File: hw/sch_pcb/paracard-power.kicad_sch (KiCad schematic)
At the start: 1 part, among them P3 BTH-030-01-F-D-A

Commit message: Update schematics. Preparation to resolve #2.
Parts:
- P3: footprint CONN_SAMTEC_BTH_60 -> Mlab_CON:SAMTEC-BTH-030-01-X-D-A; symbol adapteva_kicad:CONN_SAMTEC_BTH_60 -> MLAB_CONNECTORS:CONN_SAMTEC_BTH_030
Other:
- company: ORBISYS www.orbisys.sk -> MLAB.cz
- title: MPPB01A -> MPPB01B
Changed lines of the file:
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@@
   (paper "B")
   (title_block
-    (title "MPPB01A")
-    (date "09 May 2014")
-    (rev "REV 0.1")
-    (company "ORBISYS www.orbisys.sk")
+    (title "MPPB01B")
+    (date "2022-03-24")
+    (company "MLAB.cz")
     (comment 1 "VERSION 1")
     (comment 2 "Paralella reduction board")
-    (comment 3 "Maksim Rezenov, Jakub kakona")
+    (comment 3 "Maksim Rezenov, Jakub Kakona")
   )
   (junction (at 214.63 116.84) (diameter 0) (color 0 0 0 0)
@@
     (pin "1")
   )
-  (symbol (lib_id "adapteva_kicad:CONN_SAMTEC_BTH_60") (at 232.41 128.27 0) (unit 1)
+  (symbol (lib_id "MLAB_CONNECTORS:CONN_SAMTEC_BTH_030") (at 232.41 128.27 0) (unit 1)
     (in_bom yes) (on_board yes)
     (property "Reference" "P3" (id 0) (at 232.41 85.09 0)
@@
       (effects (font (size 1.524 1.524)))
     )
-    (property "Footprint" "CONN_SAMTEC_BTH_60" (id 2) (at 234.95 128.27 90)
+    (property "Footprint" "Mlab_CON:SAMTEC-BTH-030-01-X-D-A" (id 2) (at 234.95 128.27 90)
       (effects (font (size 1.524 1.524)) hide)
     )
-    (property "Datasheet" "" (id 3) (at 234.95 105.41 0)
+    (property "Datasheet" "https://cz.mouser.com/datasheet/2/527/bth-2498158.pdf" (id 3) (at 234.95 105.41 0)
       (effects (font (size 1.524 1.524)) hide)
     )

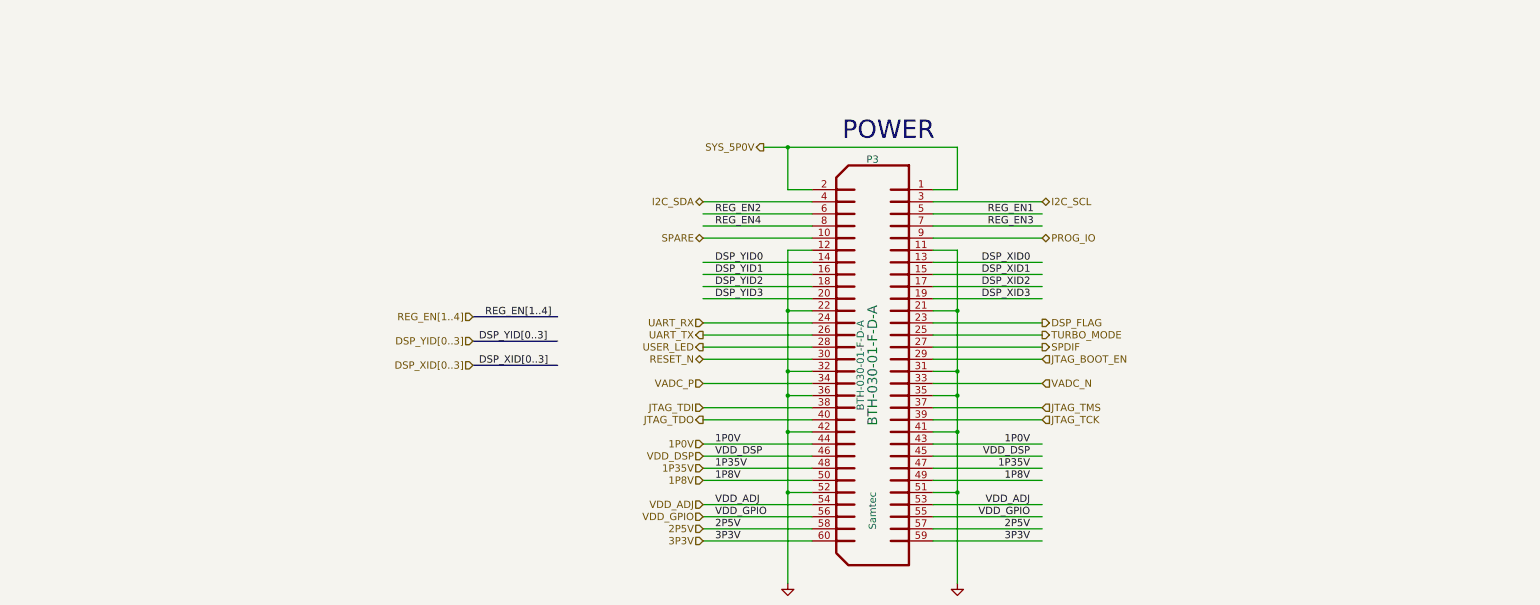
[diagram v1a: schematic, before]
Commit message: Adding pull-up resistor to resolve #1.
Geometric preparation for #2.
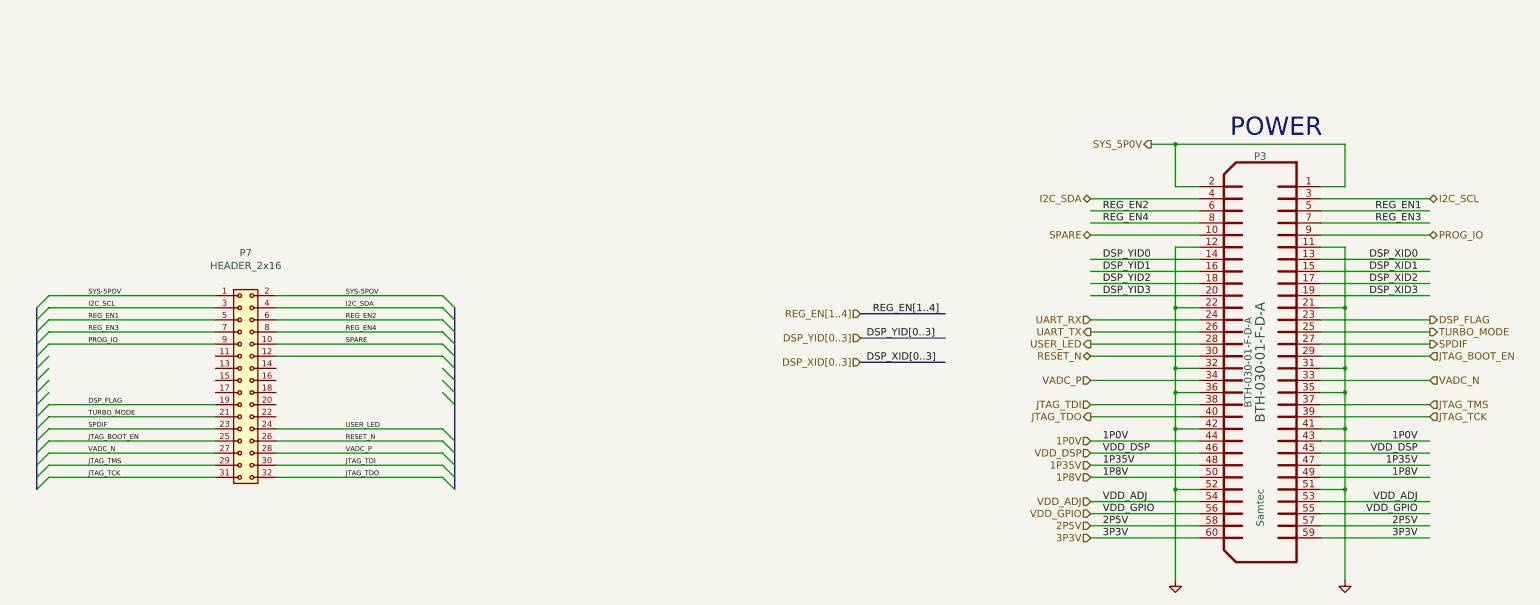
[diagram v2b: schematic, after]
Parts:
- added P7: HEADER_2x16, Mlab_Pin_Headers:Straight_2x16, symbol MLAB_HEADER:HEADER_2x16
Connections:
- net DSP_FLAG: now also P7.19
- net I2C_SCL: now also P7.3
- net I2C_SDA: now also P7.4
- net JTAG_BOOT_EN: now also P7.25
- net JTAG_TCK: now also P7.31
- net JTAG_TDI: now also P7.30
- net JTAG_TDO: now also P7.32
- net JTAG_TMS: now also P7.29
- net PROG_IO: now also P7.9
- net REG_EN1: now also P7.5
- net REG_EN2: now also P7.6
- net REG_EN3: now also P7.7
- net REG_EN4: now also P7.8
- net RESET_N: now also P7.26
- net SPARE: now also P7.10
- net SPDIF: now also P7.23
- net TURBO_MODE: now also P7.21
- net USER_LED: now also P7.24
- net VADC_N: now also P7.27
- net VADC_P: now also P7.28
- new net SYS-5POV: P7.1, P7.2
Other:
- moved on the sheet: P3

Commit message: Improve connector pinout #2
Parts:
- added P11: HEADER_2x05_PARALLEL, Mlab_Pin_Headers:Straight_2x05, symbol MLAB_HEADER:HEADER_2x05_PARALLEL
- added R3: 10k, Resistor_SMD:R_0805_2012Metric_Pad1.20x1.40mm_HandSolder, symbol paracard-template-rescue:R-device
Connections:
- net 2P5V: now also P7.12
- net 3P3V: now also P7.6
- net GND: now also P7.5, P11.1, P11.10, P11.2, P11.9
- net I2C_SCL: now also P11.3, P11.4; no longer P7.3
- net I2C_SDA: now also P11.7, P11.8; no longer P7.4
- net REG_EN1: no longer P7.5
- net REG_EN2: no longer P7.6
- net SPARE: no longer P3.10 (P10)
- net SYS-5POV: now also P11.5, P11.6
- net UART_RX: now also P7.3, R3.2
- net UART_TX: now also P7.4
- net VDD_ADJ: now also P7.14, R3.1
- net VDD_GPIO: now also P7.16
- no-connect marks 0 -> 1

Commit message: routing cest ke konektoru
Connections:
- net DSP_FLAG: now also P7.31; no longer P7.19
- net JTAG_TCK: now also P7.19; no longer P7.31
- net JTAG_TMS: now also P7.23; no longer P7.29
- net SPDIF: now also P7.27; no longer P7.23
- net TURBO_MODE: now also P7.29; no longer P7.21
- net VADC_N: now also P7.21; no longer P7.27
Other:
- moved on the sheet: P7, R3

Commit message: uprava pinoutu konektoru
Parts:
- removed P7: HEADER_2x16, Mlab_Pin_Headers:Straight_2x16, symbol MLAB_HEADER:HEADER_2x16
- added P7: HEADER_2x13, Mlab_Pin_Headers:Straight_2x13, symbol MLAB_HEADER:HEADER_2x13
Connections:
- net 2P5V: now also P7.12
- net 3P3V: now also P7.6, P7.8
- net DSP_FLAG: now also P7.25
- net GND: now also P7.5, P7.7
- net JTAG_BOOT_EN: now also P7.19
- net JTAG_TCK: now also P7.13
- net JTAG_TDI: now also P7.14
- net JTAG_TDO: now also P7.16
- net JTAG_TMS: now also P7.15
- net PROG_IO: now also P7.11
- net REG_EN3: now also P7.9
- net REG_EN4: now also P7.10
- net RESET_N: now also P7.20
- net SPDIF: now also P7.21
- net SYS-5POV: now also P7.1, P7.2
- net TURBO_MODE: now also P7.23
- net UART_RX: now also P7.3
- net UART_TX: now also P7.4
- net USER_LED: now also P7.18
- net VADC_N: now also P7.17
- net VADC_P: now also P7.22
- net VDD_ADJ: now also P7.24
- net VDD_GPIO: now also P7.26
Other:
- moved on the sheet: R3

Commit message: Routovani cesticek, uprava pinoutu
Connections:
- net SYS-5POV is gone; now on net SYS_5P0V: P11.5, P11.6, P7.1, P7.2
- net 3P3V: now also P7.3, P7.4; no longer P7.6, P7.8
- net GND: now also P7.6; no longer P7.7
- net SPDIF: now also P7.17; no longer P7.21
- net UART_RX: now also P7.7; no longer P7.3
- net UART_TX: now also P7.8; no longer P7.4
- net VADC_N: now also P7.21; no longer P7.17

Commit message: pridani UST_ID
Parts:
- R3: UST_ID (none) -> 5c70984612875079b91f899f
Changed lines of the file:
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@@
+      (effects (font (size 1.27 1.27)) hide)
+    )
+    (property "UST_ID" "5c70984612875079b91f899f" (id 4) (at 91.44 101.6 0)
       (effects (font (size 1.27 1.27)) hide)
     )

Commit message: Priprava pro osazeni
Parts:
- P11: value HEADER_2x05_PARALLEL -> (none); footprint Mlab_Pin_Headers:Straight_2x05 -> (none)
- P3: value BTH-030-01-F-D-A -> (none); footprint Mlab_CON:SAMTEC-BTH-030-01-X-D-A -> (none); UST_ID (none) -> 628e4f00243ef5997b12f43c
- P7: value HEADER_2x13 -> (none); footprint Mlab_Pin_Headers:Straight_2x13 -> (none)
- R3: value 10k -> (none); footprint Resistor_SMD:R_0805_2012Metric_Pad1.20x1.40mm_HandSolder -> (none)
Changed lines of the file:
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@@
       (effects (font (size 1.524 1.524)))
     )
-    (property "Value" "BTH-030-01-F-D-A" (id 1) (at 311.15 127.635 90)
-      (effects (font (size 1.524 1.524)))
-    )
-    (property "Footprint" "Mlab_CON:SAMTEC-BTH-030-01-X-D-A" (id 2) (at 316.23 127.635 90)
+    (property "Value" "" (id 1) (at 311.15 127.635 90)
+      (effects (font (size 1.524 1.524)))
+    )
+    (property "Footprint" "" (id 2) (at 316.23 127.635 90)
       (effects (font (size 1.524 1.524)) hide)
     )
@@
     (property "Manufacturer" "Samtec" (id 5) (at 313.69 158.115 90)
       (effects (font (size 1.524 1.524)))
+    )
+    (property "UST_ID" "628e4f00243ef5997b12f43c" (id 6) (at 313.69 127.635 0)
+      (effects (font (size 1.27 1.27)) hide)
     )
     (pin "1")
@@
       (effects (font (size 1.524 1.524)))
     )
-    (property "Value" "HEADER_2x13" (id 1) (at 101.6 107.95 0)
-      (effects (font (size 1.524 1.524)))
-    )
-    (property "Footprint" "Mlab_Pin_Headers:Straight_2x13" (id 2) (at 101.6 110.49 0)
+    (property "Value" "" (id 1) (at 101.6 107.95 0)
+      (effects (font (size 1.524 1.524)))
+    )
+    (property "Footprint" "" (id 2) (at 101.6 110.49 0)
       (effects (font (size 1.524 1.524)) hide)
     )
@@
       (effects (font (size 1.524 1.524)) (justify left))
     )
-    (property "Value" "HEADER_2x05_PARALLEL" (id 1) (at 99.7712 64.0842 0)
+    (property "Value" "" (id 1) (at 99.7712 64.0842 0)
       (effects (font (size 1.524 1.524)) (justify left) hide)
     )
-    (property "Footprint" "Mlab_Pin_Headers:Straight_2x05" (id 2) (at 96.52 57.785 0)
+    (property "Footprint" "" (id 2) (at 96.52 57.785 0)
       (effects (font (size 1.524 1.524)) hide)
     )
@@
     (in_bom yes) (on_board yes)
     (property "Reference" "R3" (id 0) (at 88.9 101.6 90))
-    (property "Value" "10k" (id 1) (at 91.44 101.6 90))
-    (property "Footprint" "Resistor_SMD:R_0805_2012Metric_Pad1.20x1.40mm_HandSolder" (id 2) (at 89.662 101.6 90)
-      (effects (font (size 1.27 1.27)) hide)
-    )
+    (property "Value" "" (id 1) (at 91.44 101.6 90))
+    (property "Footprint" "" (id 2) (at 89.662 101.6 90)
+      (effects (font (size 1.27 1.27)) hide)
+    )
